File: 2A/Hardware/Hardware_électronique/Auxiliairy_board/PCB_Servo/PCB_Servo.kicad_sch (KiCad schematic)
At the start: 35 parts, among them J10 Conn_ST_STDC14, J9 UART_IN, U1 STM32G071CBUx, U2 AZ1117-3.3

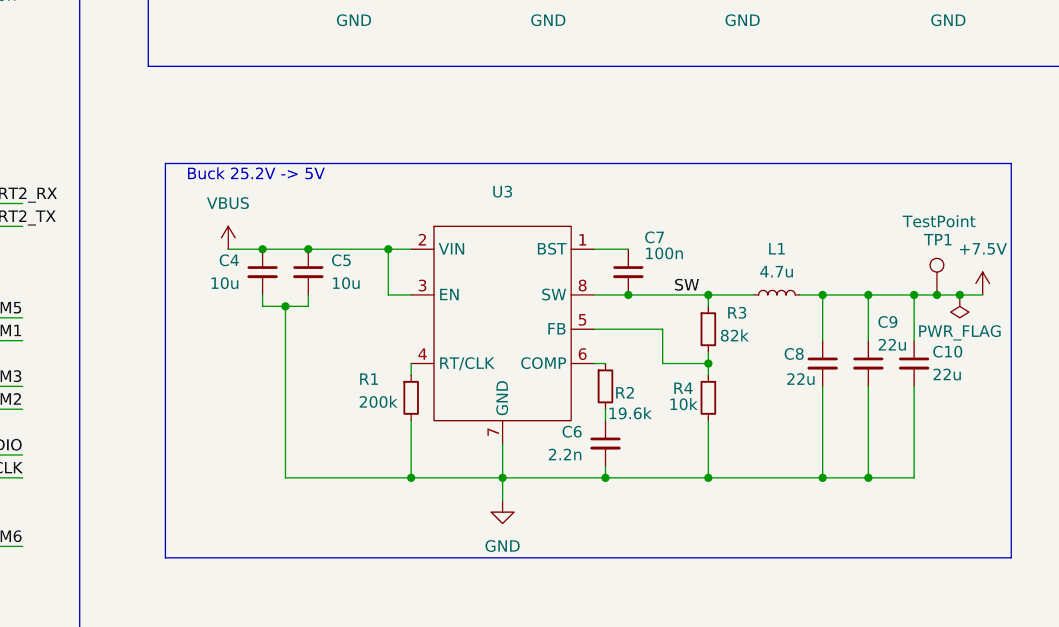
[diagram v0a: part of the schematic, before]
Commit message: Correction PCB Servo LF
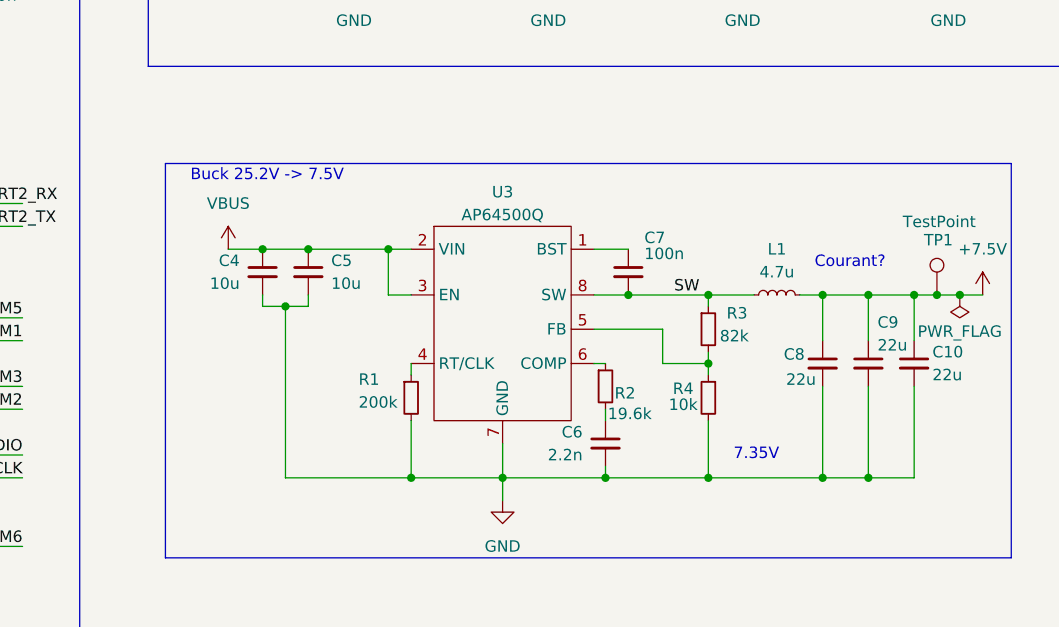
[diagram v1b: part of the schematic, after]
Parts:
- U3: value ~ -> AP64500Q
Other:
- note added: "7.35V"
- note added: "Buck 25.2V -> 7.5V"
- note added: "Courant?"
- note removed: "Buck 25.2V -> 5V"
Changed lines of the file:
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@@
 		)
 	)
-	(text "Buck 25.2V -> 5V"
+	(text "Buck 25.2V -> 7.5V"
 		(exclude_from_sim no)
-		(at 193.548 74.422 0)
+		(at 194.818 74.422 0)
+		(effects
+			(font
+				(size 1.27 1.27)
+			)
+		)
+	)
+	(text "7.35V"
+		(exclude_from_sim no)
+		(at 249.174 105.41 0)
+		(effects
+			(font
+				(size 1.27 1.27)
+			)
+		)
+	)
+	(text "Courant?"
+		(exclude_from_sim no)
+		(at 259.588 84.074 0)
 		(effects
 			(font
@@
 			)
 		)
-		(property "Value" "~"
+		(property "Value" "AP64500Q"
 			(at 220.98 78.74 0)
 			(effects
@@
 		)
 		(instances
-			(project ""
+			(project "PCB_Servo"
 				(path "/7d8c2ca7-c6ac-4d1b-8da0-598ada20afbe"
 					(reference "U2")
@@
 		)
 		(instances
-			(project ""
+			(project "PCB_Servo"
 				(path "/7d8c2ca7-c6ac-4d1b-8da0-598ada20afbe"
 					(reference "C17")
